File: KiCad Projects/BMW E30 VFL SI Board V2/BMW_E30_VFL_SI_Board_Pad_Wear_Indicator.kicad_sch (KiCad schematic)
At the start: 11 parts, among them Q8 BC327-16

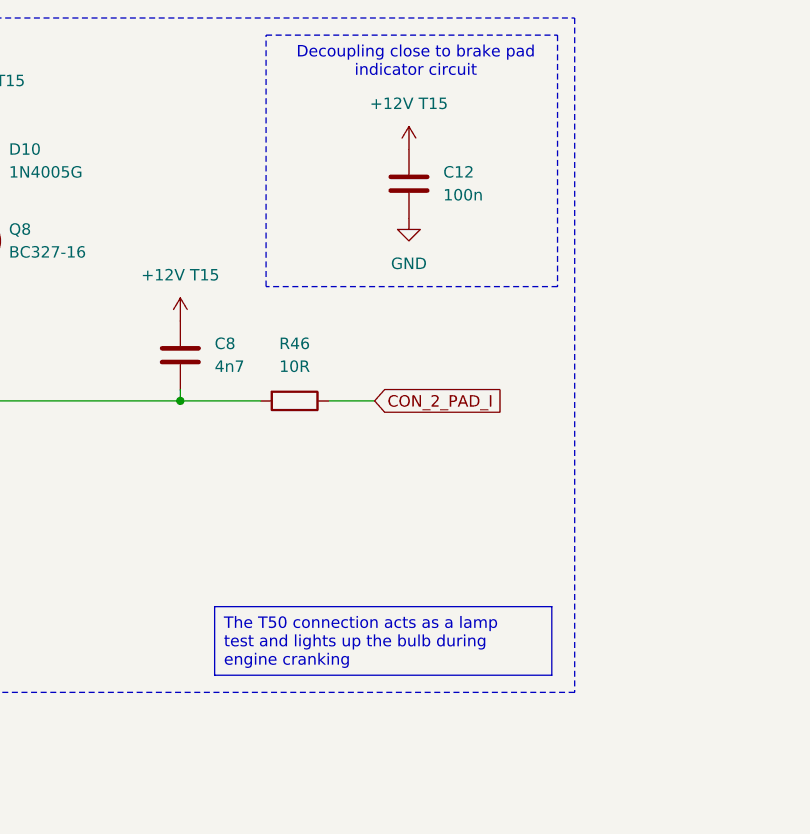
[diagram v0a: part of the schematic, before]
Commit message: V2 Board Updates
Added in extra resistors, cap, and diode that were added to a  particular version of the SI board from the USDM on the comparator circuit. Updated the schematic diagram of the comparator circuit to improve readability. Updated the clock frequency measured with a scope. Made a few minor layout improvements including moving the "JP" connections inwards as not to interfere with the plastic housing for the PCB in the cluster and other minor layout errors such as swapped reference designators. Updated info on where the +5V regulator gets its source voltage from. These updates are reflected in schematic version V2.1 as denoted in the title box (not in the title of the schematic file).
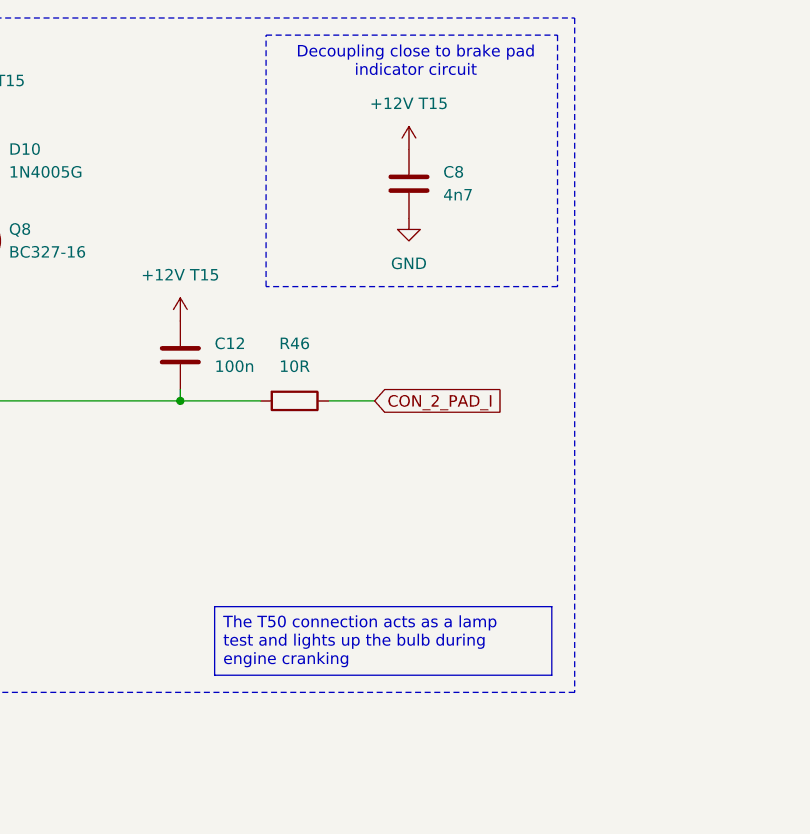
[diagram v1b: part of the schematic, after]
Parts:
- C12: renamed from C8; value 4n7 -> 100n
- C8: renamed from C12; value 100n -> 4n7
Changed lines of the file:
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@@
 (kicad_sch
-	(version 20231120)
+	(version 20250114)
 	(generator "eeschema")
-	(generator_version "8.0")
+	(generator_version "9.0")
 	(paper "A4")
 	(title_block
@@
 		(date "2024-06-15")
 		(rev "2")
+		(comment 1 "Revision 2.1 made by Reagan Ansel")
+	)
+	(rectangle
+		(start 182.245 53.34)
+		(end 214.63 81.28)
+		(stroke
+			(width 0)
+			(type dash)
+		)
+		(fill
+			(type none)
+		)
+	)
+	(rectangle
+		(start 71.12 51.435)
+		(end 216.535 126.365)
+		(stroke
+			(width 0)
+			(type dash)
+		)
+		(fill
+			(type none)
+		)
+	)
+	(text "BMW_E30_VFL_SI_Board_Pad_Wear_Indicator"
+		(exclude_from_sim no)
+		(at 228.854 173.482 0)
+		(effects
+			(font
+				(size 2.54 2.54)
+			)
+		)
+	)
+	(text "Brake pad wear indicator"
+		(exclude_from_sim no)
+		(at 85.852 55.118 0)
+		(effects
+			(font
+				(size 1.27 1.27)
+			)
+		)
+	)
+	(text "Decoupling close to brake pad \nindicator circuit"
+		(exclude_from_sim no)
+		(at 198.882 56.388 0)
+		(effects
+			(font
+				(size 1.27 1.27)
+			)
+		)
+	)
+	(text_box "The T50 connection acts as a lamp test and lights up the bulb during engine cranking"
+		(exclude_from_sim no)
+		(at 176.53 116.84 0)
+		(size 37.465 7.62)
+		(margins 0.9525 0.9525 0.9525 0.9525)
+		(stroke
+			(width 0)
+			(type default)
+		)
+		(fill
+			(type color)
+			(color 255 239 232 1)
+		)
+		(effects
+			(font
+				(size 1.27 1.27)
+			)
+			(justify left top)
+		)
 	)
 	(junction
@@
 		)
 	)
-	(rectangle
-		(start 182.245 53.34)
-		(end 214.63 81.28)
-		(stroke
-			(width 0)
-			(type dash)
-		)
-		(fill
-			(type none)
-		)
-	)
-	(rectangle
-		(start 81.915 128.27)
-		(end 81.915 128.27)
-		(stroke
-			(width 0)
-			(type default)
-		)
-		(fill
-			(type none)
-		)
-	)
-	(rectangle
-		(start 71.12 51.435)
-		(end 216.535 126.365)
-		(stroke
-			(width 0)
-			(type dash)
-		)
-		(fill
-			(type none)
-		)
-	)
-	(text_box "The T50 connection acts as a lamp test and lights up the bulb during engine cranking"
-		(exclude_from_sim no)
-		(at 176.53 116.84 0)
-		(size 37.465 7.62)
-		(stroke
-			(width 0)
-			(type default)
-		)
-		(fill
-			(type color)
-			(color 255 239 232 1)
-		)
+	(global_label "CON_2_PAD_I"
+		(shape input)
+		(at 194.31 93.98 0)
+		(fields_autoplaced yes)
 		(effects
 			(font
 				(size 1.27 1.27)
 			)
-			(justify left top)
-		)
-	)
-	(text "BMW_E30_VFL_SI_Board_Pad_Wear_Indicator"
-		(exclude_from_sim no)
-		(at 228.854 173.482 0)
-		(effects
-			(font
-				(size 2.54 2.54)
-			)
-		)
-	)
-	(text "Brake pad wear indicator"
-		(exclude_from_sim no)
-		(at 85.852 55.118 0)
+			(justify left)
+		)
+		(property "Intersheetrefs" "${INTERSHEET_REFS}"
+			(at 209.5719 93.98 0)
+			(effects
+				(font
+					(size 1.27 1.27)
+				)
+				(justify left)
+				(hide yes)
+			)
+		)
+	)
+	(global_label "CON_4_PADS"
+		(shape input)
+		(at 92.71 114.3 180)
+		(fields_autoplaced yes)
 		(effects
 			(font
 				(size 1.27 1.27)
 			)
-		)
-	)
-	(text "Decoupling close to brake pad \nindicator circuit"
-		(exclude_from_sim no)
-		(at 198.882 56.388 0)
+			(justify right)
+		)
+		(property "Intersheetrefs" "${INTERSHEET_REFS}"
+			(at 77.811 114.3 0)
+			(effects
+				(font
+					(size 1.27 1.27)
+				)
+				(justify right)
+				(hide yes)
+			)
+		)
+	)
+	(global_label "CON_12_T50"
+		(shape input)
+		(at 133.35 93.98 180)
+		(fields_autoplaced yes)
 		(effects
 			(font
 				(size 1.27 1.27)
 			)
-		)
-	)
-	(global_label "CON_2_PAD_I"
+			(justify right)
+		)
+		(property "Intersheetrefs" "${INTERSHEET_REFS}"
+			(at 118.693 93.98 0)
+			(effects
+				(font
+					(size 1.27 1.27)
+				)
+				(justify right)
+				(hide yes)
+			)
+		)
+	)
+	(global_label "CON_19_PADS"
 		(shape input)
-		(at 194.31 93.98 0)
+		(at 95.25 76.2 180)
 		(fields_autoplaced yes)
 		(effects
@@
 				(size 1.27 1.27)
 			)
-			(justify left)
-		)
-		(property "Intersheetrefs" "${INTERSHEET_REFS}"
-			(at 209.5719 93.98 0)
-			(effects
-				(font
-					(size 1.27 1.27)
-				)
-				(justify left)
-				(hide yes)
-			)
-		)
-	)
-	(global_label "CON_4_PADS"
-		(shape input)
-		(at 92.71 114.3 180)
-		(fields_autoplaced yes)
-		(effects
-			(font
-				(size 1.27 1.27)
-			)
-			(justify right)
-		)
-		(property "Intersheetrefs" "${INTERSHEET_REFS}"
-			(at 77.811 114.3 0)
-			(effects
-				(font
-					(size 1.27 1.27)
-				)
-				(justify right)
-				(hide yes)
-			)
-		)
-	)
-	(global_label "CON_12_T50"
-		(shape input)
-		(at 133.35 93.98 180)
-		(fields_autoplaced yes)
-		(effects
-			(font
-				(size 1.27 1.27)
-			)
-			(justify right)
-		)
-		(property "Intersheetrefs" "${INTERSHEET_REFS}"
-			(at 118.693 93.98 0)
-			(effects
-				(font
-					(size 1.27 1.27)
-				)
-				(justify right)
-				(hide yes)
-			)
-		)
-	)
-	(global_label "CON_19_PADS"
-		(shape input)
-		(at 95.25 76.2 180)
-		(fields_autoplaced yes)
-		(effects
-			(font
-				(size 1.27 1.27)
-			)
 			(justify right)
 		)
@@
 		(dnp no)
 		(fields_autoplaced yes)
-		(property "Reference" "C8"
+		(property "Reference" "C12"
 			(at 176.53 87.6299 0)
 			(effects
@@
 			)
 		)
-		(property "Value" "4n7"
+		(property "Value" "100n"
 			(at 176.53 90.1699 0)
 			(effects
@@
 			(project "BMW E30 VFL SI Board V2"
 				(path "/b9f8b657-f23f-4f46-b33b-c9c07ea00dca/06cb897c-0efb-438a-95e3-30e073586624"
-					(reference "C8")
+					(reference "C12")
 					(unit 1)
 				)
@@
 		(dnp no)
 		(fields_autoplaced yes)
-		(property "Reference" "C12"
+		(property "Reference" "C8"
 			(at 201.93 68.5799 0)
 			(effects
@@
 			)
 		)
-		(property "Value" "100n"
+		(property "Value" "4n7"
 			(at 201.93 71.1199 0)
 			(effects
@@
 			(project "BMW E30 VFL SI Board V2"
 				(path "/b9f8b657-f23f-4f46-b33b-c9c07ea00dca/06cb897c-0efb-438a-95e3-30e073586624"
-					(reference "C12")
-					(unit 1)
-				)
+					(reference "C8")
+					(unit 1)
+				)
